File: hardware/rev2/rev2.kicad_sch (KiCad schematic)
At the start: 31 parts, among them J1 USB_C_Receptacle_USB2.0_16P, J2 uFL, J3 uFL, J4 Antenna RF and GNSS Data, J5 Antenna GND, U1 EClamp2522P

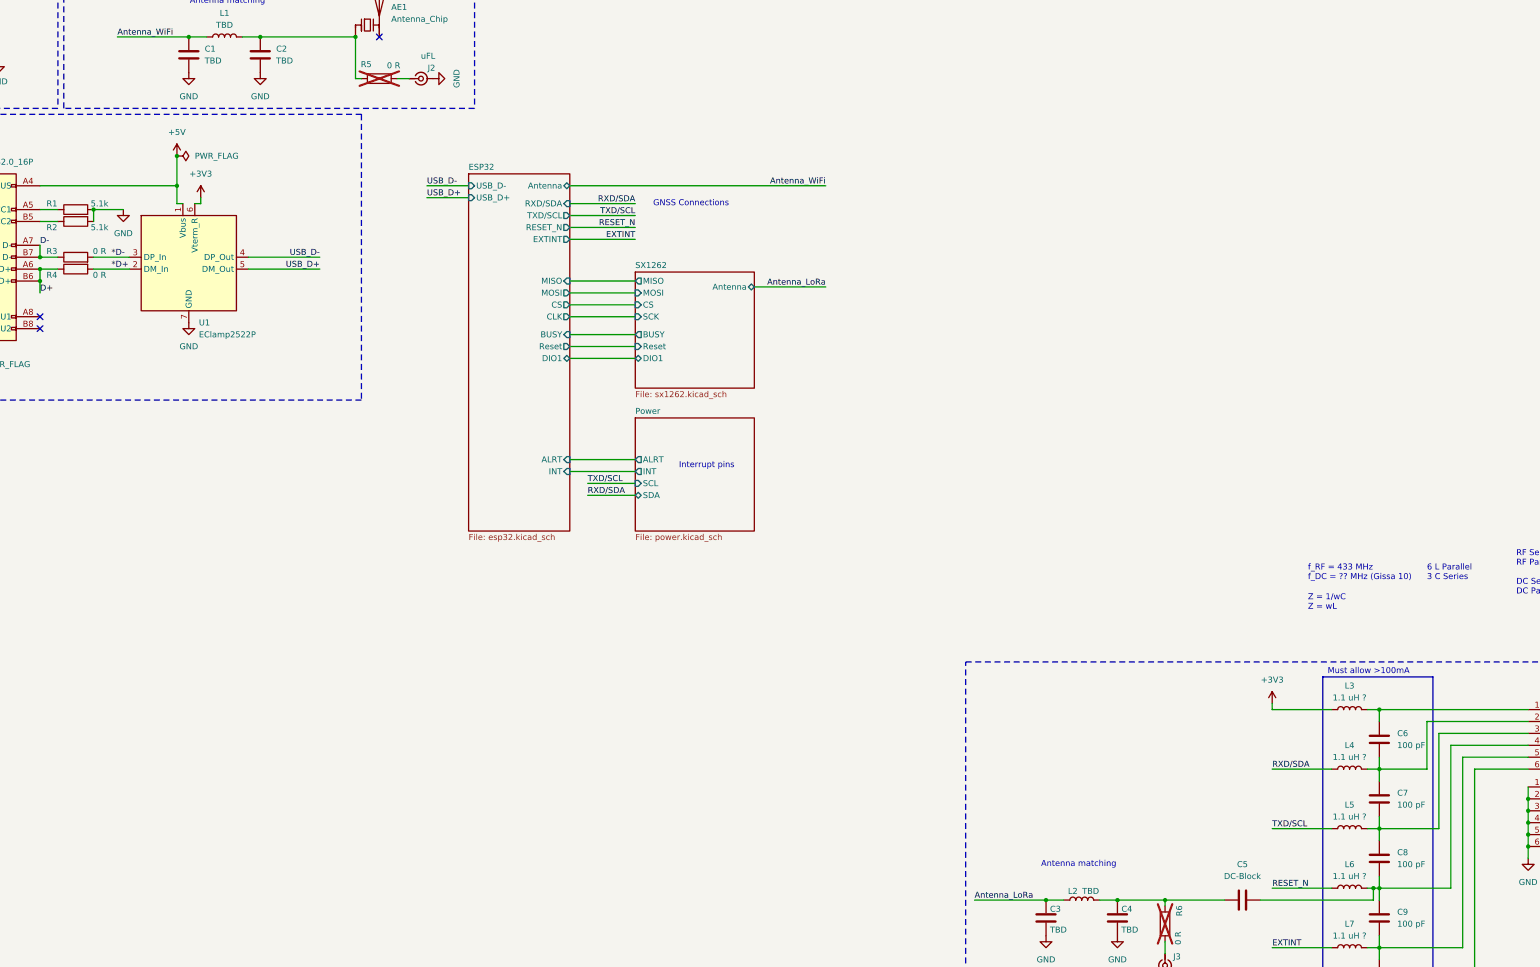
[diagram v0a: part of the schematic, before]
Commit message: added testpoints, added LEDs, fixed a lot of DRC stuff
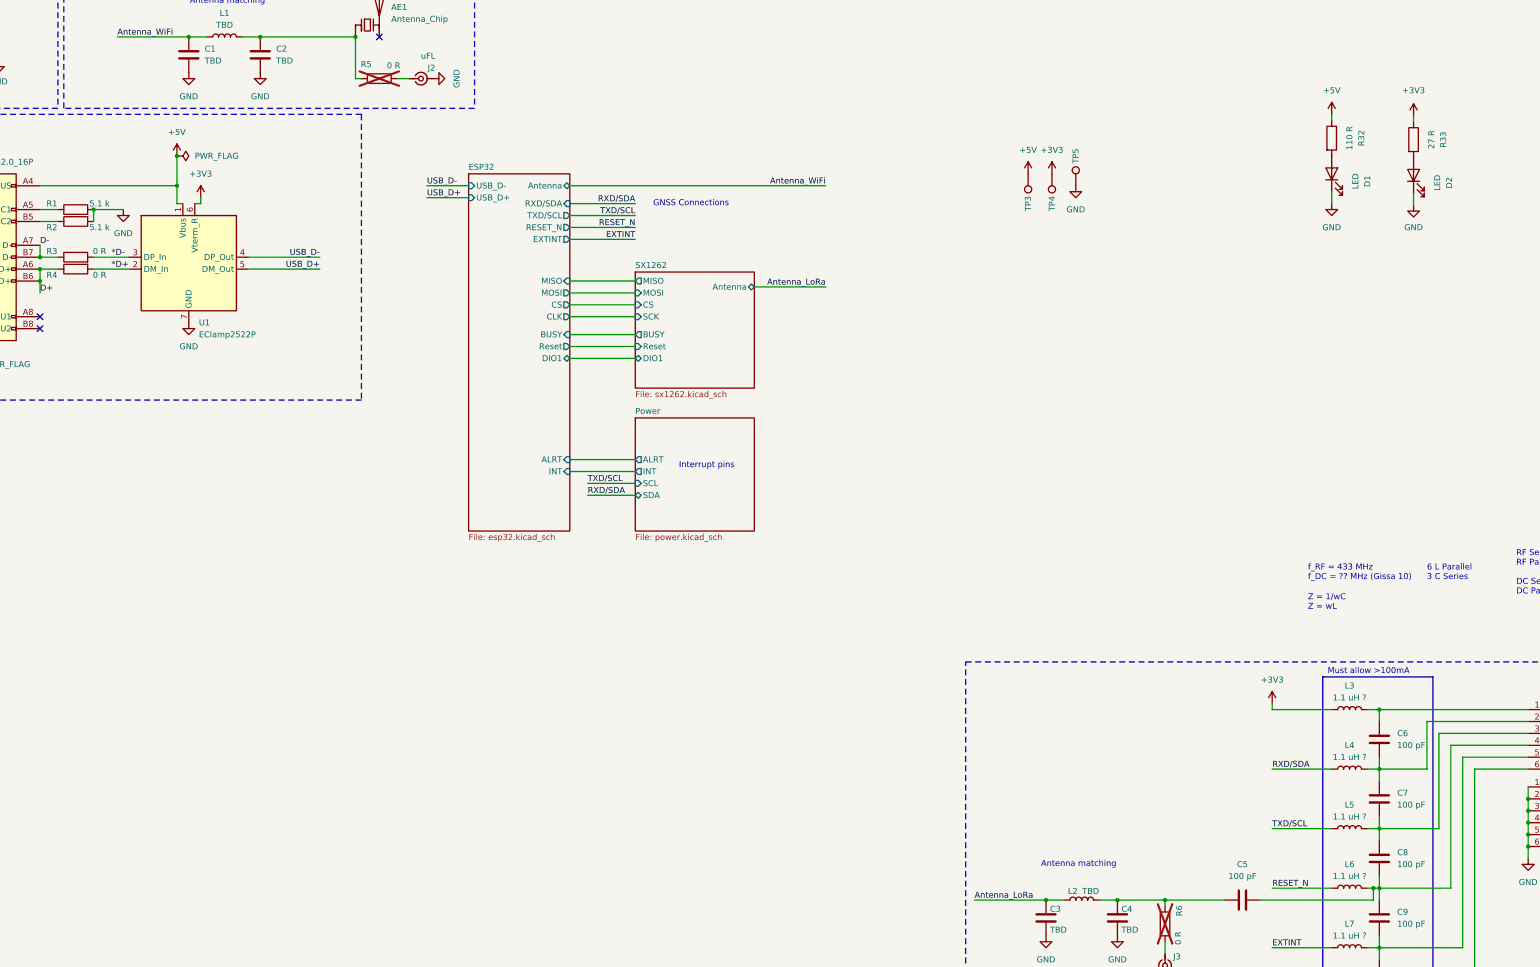
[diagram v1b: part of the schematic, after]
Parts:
- added D1, D2: LED, LED_SMD:LED_0603_1608Metric_Pad1.05x0.95mm_HandSolder, symbol Device:LED
- added R32: 110 R, Resistor_SMD:R_0603_1608Metric_Pad0.98x0.95mm_HandSolder, symbol Device:R
- added R33: 27 R, Resistor_SMD:R_0603_1608Metric_Pad0.98x0.95mm_HandSolder, symbol Device:R
- added TP3, TP4, TP5: TestPoint, TestPoint:TestPoint_Pad_D1.0mm, symbol Connector:TestPoint
- C5: value DC-Block -> 100 pF
- L3, L4, L5, L6, L7, L8: Mouser Part Number 710-744230251 ? -> (none)
- R1, R2: value 5.1k -> 5.1 k; footprint Inductor_SMD:L_0603_1608Metric_Pad1.05x0.95mm_HandSolder -> Resistor_SMD:R_0603_1608Metric_Pad0.98x0.95mm_HandSolder; Mouser Part Number (none) -> 71-CRCW0603J-5.1K-E3
- R5, R6: Mouser Part Number 71-CRCW04020000Z0EDC -> 71-CRCW04020000Z0EDC
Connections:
- net +3V3: now also R33.1, TP4.1
- net +5V: now also R32.1, TP3.1
- net GND: now also D1.1 (K), D2.1 (K), TP5.1
- new net: D2.2 (A), R33.2
- new net: D1.2 (A), R32.2

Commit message: set mouser part number to tweezer so I don't forgor
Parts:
- J4: Mouser Part Number (none) -> 910-CQ-ESD-10
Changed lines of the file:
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@@
+			)
+		)
+		(property "Mouser Part Number" "910-CQ-ESD-10"
+			(at 369.57 173.99 0)
+			(hide yes)
+			(show_name no)
+			(do_not_autoplace no)
+			(effects
+				(font
+					(size 1.27 1.27)
+				)
 			)
 		)

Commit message: changed layout a bit, updated footprints, did stuff
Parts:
- added R36: 0 R, Resistor_SMD:R_0402_1005Metric_Pad0.72x0.64mm_HandSolder, symbol Device:R
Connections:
- net at C4.1, L2.1, R6.1: now also R36.1; no longer C5.1
- net RXD/SDA renamed SDA
- net TXD/SCL renamed SCL
- new net: C5.1, R36.2
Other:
- sheet ESP32 ports: added SCL, SDA; removed RXD/SDA, TXD/SCL
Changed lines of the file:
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@@
 	)
 	(junction
+		(at 287.02 209.55)
+		(diameter 0)
+		(color 0 0 0 0)
+	)
+	(junction
 		(at 261.62 209.55)
 		(diameter 0)
@@
 	)
 	(junction
-		(at 287.02 209.55)
-		(diameter 0)
-		(color 0 0 0 0)
-	)
-	(junction
 		(at 78.74 25.4)
 		(diameter 0)
@@
 	(wire
 		(pts
+			(xy 287.02 209.55) (xy 289.56 209.55)
+		)
+		(stroke
+			(width 0)
+			(type default)
+		)
+	)
+	(wire
+		(pts
 			(xy 50.8 62.23) (xy 46.99 62.23)
 		)
@@
 	(wire
 		(pts
-			(xy 287.02 209.55) (xy 299.72 209.55)
-		)
-		(stroke
-			(width 0)
-			(type default)
-		)
-	)
-	(wire
-		(pts
 			(xy 332.74 168.91) (xy 332.74 171.45)
 		)
@@
 	(wire
 		(pts
+			(xy 297.18 209.55) (xy 299.72 209.55)
+		)
+		(stroke
+			(width 0)
+			(type default)
+		)
+	)
+	(wire
+		(pts
 			(xy 160.02 80.01) (xy 173.99 80.01)
 		)
@@
 		)
 	)
-	(label "RXD{slash}SDA"
+	(label "SDA"
 		(at 173.99 60.96 180)
 		(effects
@@
 		)
 	)
-	(label "RXD{slash}SDA"
+	(label "SDA"
 		(at 309.88 181.61 0)
 		(effects
@@
 		)
 	)
-	(label "TXD{slash}SCL"
+	(label "SCL"
 		(at 309.88 194.31 0)
 		(effects
@@
 		)
 	)
-	(label "RXD{slash}SDA"
+	(label "SDA"
 		(at 163.83 123.19 0)
 		(effects
@@
 		)
 	)
-	(label "TXD{slash}SCL"
+	(label "SCL"
 		(at 173.99 63.5 180)
 		(effects
@@
 		)
 	)
-	(label "TXD{slash}SCL"
+	(label "SCL"
 		(at 163.83 120.65 0)
 		(effects
@@
 		(length 1.27)
 		(shape round)
+		(at 298.45 209.55 0)
+		(fields_autoplaced yes)
+		(effects
+			(font
+				(size 1.27 1.27)
+			)
+			(justify left bottom)
+		)
+		(property "Net Class" "50 Ohm"
+			(at 299.1485 208.28 0)
+			(hide yes)
+			(show_name no)
+			(do_not_autoplace no)
+			(effects
+				(font
+					(size 1.27 1.27)
+				)
+				(justify left)
+			)
+		)
+		(property "Component Class" ""
+			(at 167.005 136.525 0)
+			(show_name no)
+			(do_not_autoplace no)
+			(effects
+				(font
+					(size 1.27 1.27)
+					(italic yes)
+				)
+			)
+		)
+	)
+	(netclass_flag ""
+		(length 1.27)
+		(shape round)
 		(at 38.1 27.94 0)
 		(effects
@@
 	)
 	(symbol
+		(lib_id "Device:R")
+		(at 293.37 209.55 90)
+		(unit 1)
+		(body_style 1)
+		(exclude_from_sim no)
+		(in_bom yes)
+		(on_board yes)
+		(in_pos_files yes)
+		(dnp no)
+		(property "Reference" "R36"
+			(at 290.576 206.502 90)
+			(show_name no)
+			(do_not_autoplace no)
+			(effects
+				(font
+					(size 1.27 1.27)
+				)
+			)
+		)
+		(property "Value" "0 R"
+			(at 296.418 206.756 90)
+			(show_name no)
+			(do_not_autoplace no)
+			(effects
+				(font
+					(size 1.27 1.27)
+				)
+			)
+		)
+		(property "Footprint" "Resistor_SMD:R_0402_1005Metric_Pad0.72x0.64mm_HandSolder"
+			(at 293.37 211.328 90)
+			(hide yes)
+			(show_name no)
+			(do_not_autoplace no)
+			(effects
+				(font
+					(size 1.27 1.27)
+				)
+			)
+		)
+		(property "Datasheet" "https://www.vishay.com/docs/20035/dcrcwe3.pdf"
+			(at 293.37 209.55 0)
+			(hide yes)
+			(show_name no)
+			(do_not_autoplace no)
+			(effects
+				(font
+					(size 1.27 1.27)
+				)
+			)
+		)
+		(property "Description" "Resistor"
+			(at 293.37 209.55 0)
+			(hide yes)
+			(show_name no)
+			(do_not_autoplace no)
+			(effects
+				(font
+					(size 1.27 1.27)
+				)
+			)
+		)
+		(property "Mouser Part Number" "71-CRCW04020000Z0EDC"
+			(at 293.37 209.55 90)
+			(hide yes)
+			(show_name no)
+			(do_not_autoplace no)
+			(effects
+				(font
+					(size 1.27 1.27)
+				)
+			)
+		)
+		(property "Sim.Type" ""
+			(at 293.37 209.55 90)
+			(hide yes)
+			(show_name no)
+			(do_not_autoplace no)
+			(effects
+				(font
+					(size 1.27 1.27)
+				)
+			)
+		)
+		(pin "1"
+		)
+		(pin "2"
+		)
+		(instances
+			(project "rev2"
+				(path "/9067f306-e23c-4d77-8182-4fa2c4b88902"
+					(reference "R36")
+					(unit 1)
+				)
+			)
+		)
+	)
+	(symbol
 		(lib_id "power:GND")
 		(at 364.49 200.66 0)
@@
 			)
 		)
-		(pin "RXD{slash}SDA" input
-			(at 160.02 60.96 0)
+		(pin "ALRT" input
+			(at 160.02 115.57 0)
 			(effects
 				(font
@@
 			)
 		)
-		(pin "TXD{slash}SCL" output
-			(at 160.02 63.5 0)
+		(pin "INT" input
+			(at 160.02 118.11 0)
 			(effects
 				(font
@@
 			)
 		)
-		(pin "ALRT" input
-			(at 160.02 115.57 0)
+		(pin "SDA" input
+			(at 160.02 60.96 0)
 			(effects
 				(font
@@
 			)
 		)
-		(pin "INT" input
-			(at 160.02 118.11 0)
+		(pin "SCL" output
+			(at 160.02 63.5 0)
 			(effects
 				(font

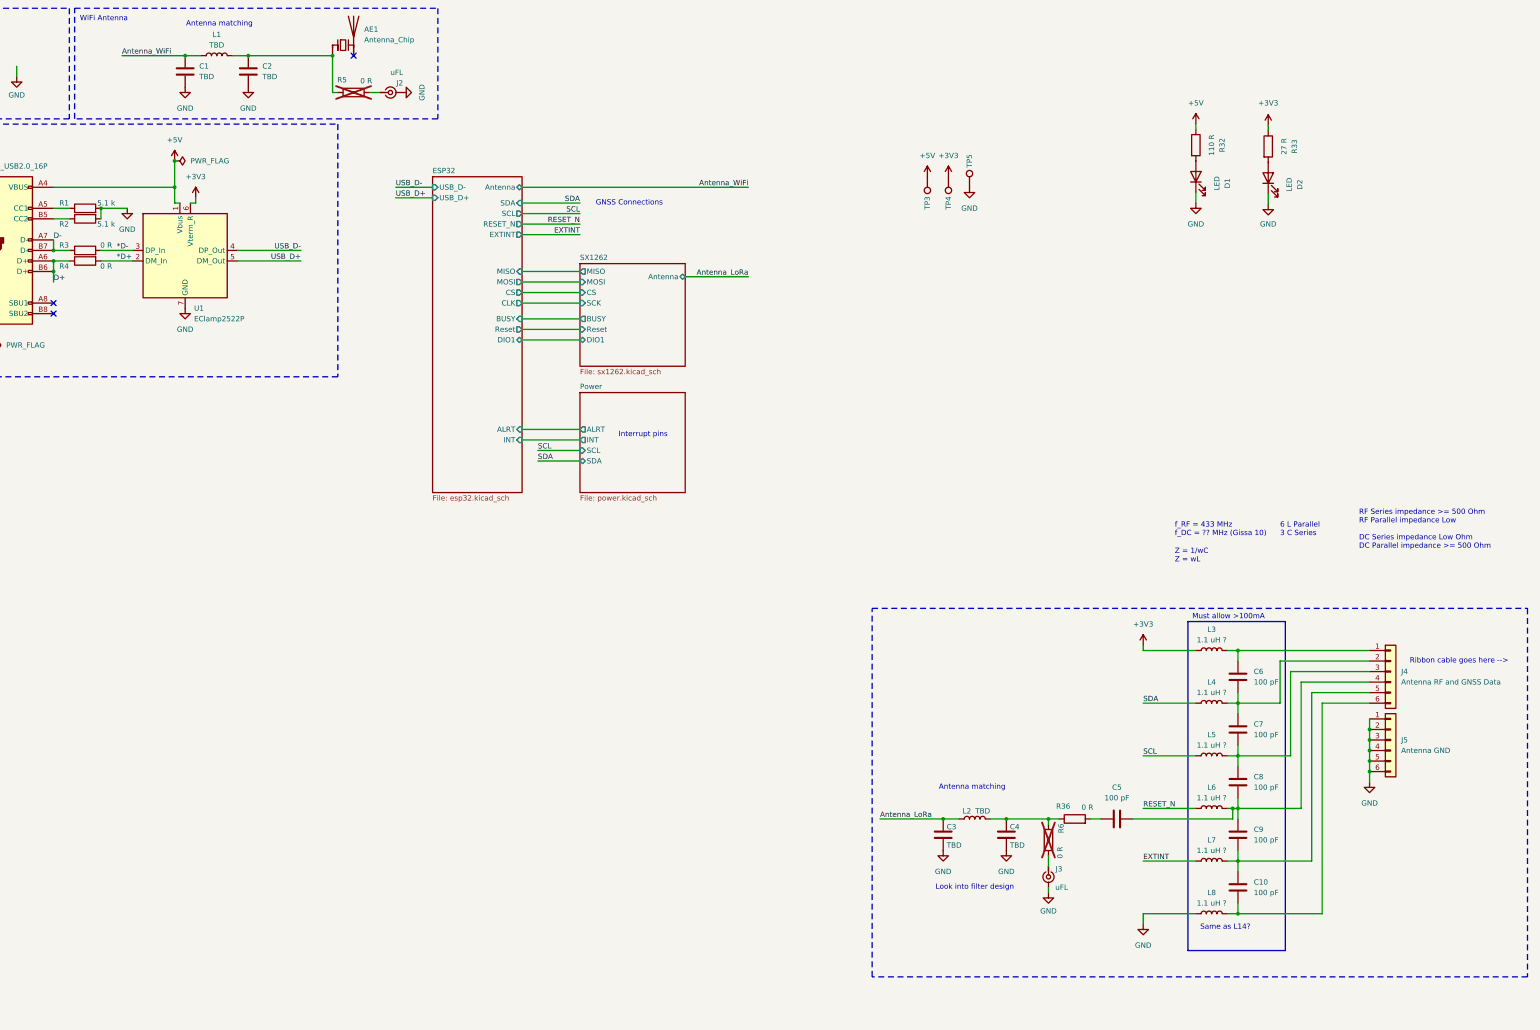
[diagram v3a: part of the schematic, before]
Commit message: finished PCB v1, changed rf connector layout, added vias, added footprints for RF filtering
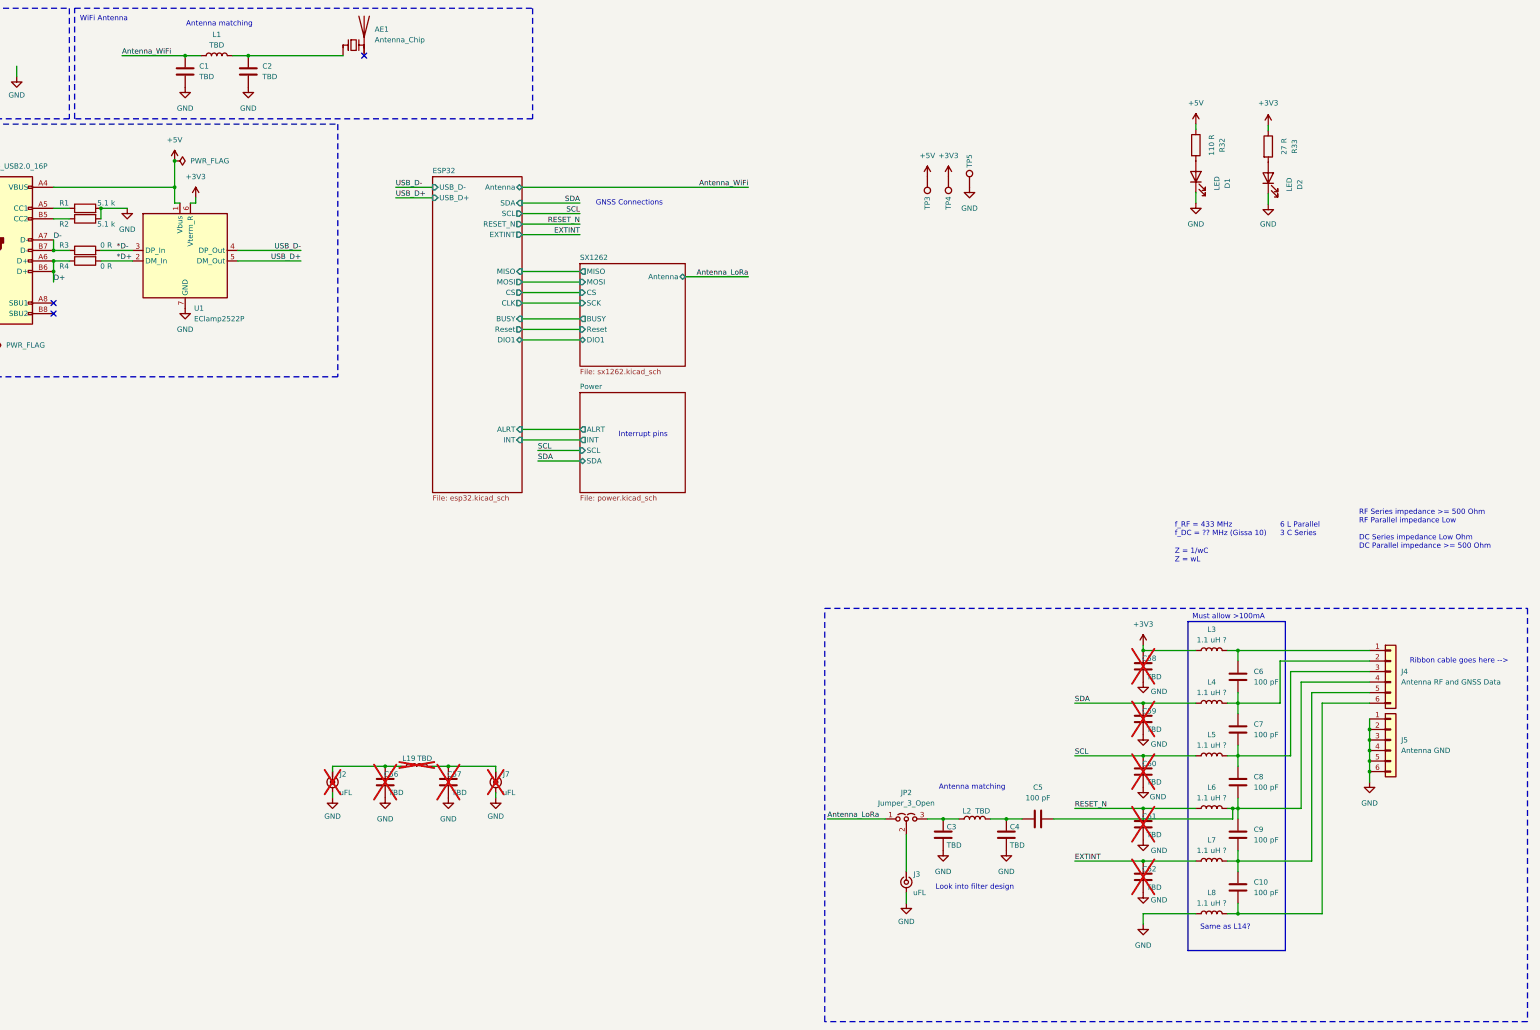
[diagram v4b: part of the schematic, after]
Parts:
- removed R36, R5, R6: 0 R, Resistor_SMD:R_0402_1005Metric_Pad0.72x0.64mm_HandSolder, symbol Device:R
- added C56, C57, C58, C59, C60, C61, C62: TBD, Capacitor_SMD:C_0402_1005Metric_Pad0.74x0.62mm_HandSolder, symbol Device:C
- added J7: uFL, _footprints:U.FL_Molex_MCRF_73412-0110_Vertical, symbol Connector:Conn_Coaxial_Small
- added JP2: Jumper_3_Open, _footprints:Jumper_3_R_0402_1005Metric_Pad0.72x0.64mm_HandSolder_Mirror, symbol Jumper:Jumper_3_Open
- added L19: TBD, Inductor_SMD:L_0402_1005Metric_Pad0.77x0.64mm_HandSolder, symbol Device:L
- J2: now not fitted
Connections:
- net +3V3: now also C58.1
- net Antenna_LoRa: now also JP2.1 (A); no longer C3.1, L2.2
- net EXTINT: now also C62.1
- net GND: now also C56.2, C57.2, C58.2, C59.2, C60.2, C61.2, C62.2, J7.2 (Ext)
- net RESET_N: now also C61.1
- net SCL: now also C60.1
- net SDA: now also C59.1
- net at C4.1, L2.1: now also C5.1
- net at J2.1 (In): now also C56.1, L19.2
- net at J3.1 (In): now also JP2.2 (C)
- new net: C3.1, JP2.3 (B), L2.2
- new net: C57.1, J7.1 (In), L19.1
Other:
- moved on the sheet: AE1, C5, J3
